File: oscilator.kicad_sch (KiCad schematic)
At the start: 5 parts, among them Y1 8Mhz

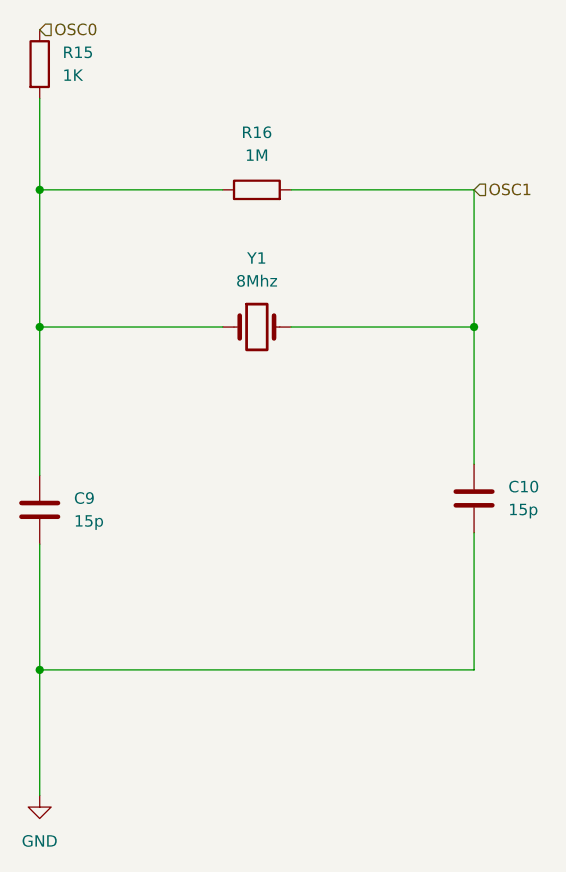
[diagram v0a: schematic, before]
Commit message: Fix KiCad 10 footprint library: register kiC library, fix schematic references
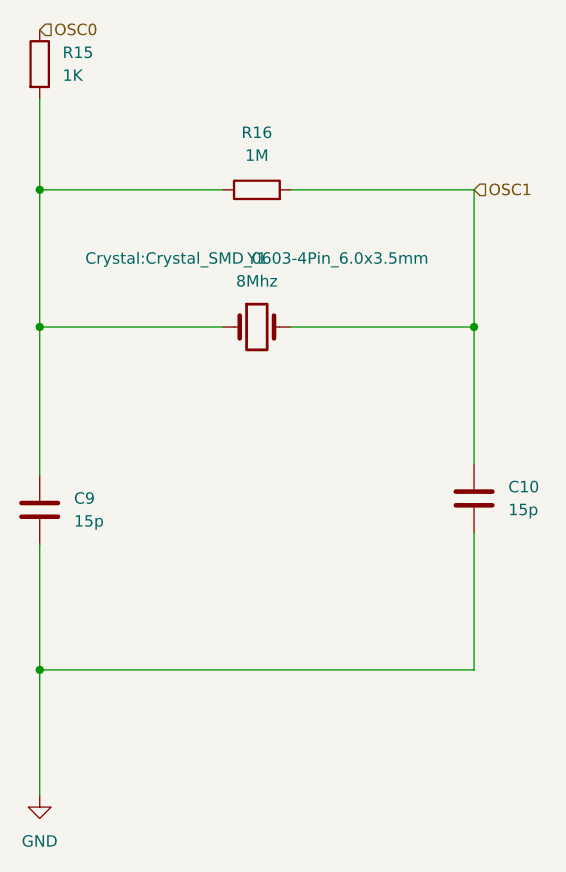
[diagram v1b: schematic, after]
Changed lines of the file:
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@@
 		(dnp no)
 		(fields_autoplaced yes)
+		(property "Footprint" "Crystal:Crystal_SMD_0603-4Pin_6.0x3.5mm"
+			(at 151.13 80.01 0)
+			(show_name no)
+			(do_not_autoplace no)
+			(effects
+				(font
+					(size 1.27 1.27)
+				)
+			)
+		)
 		(property "Reference" "Y1"
 			(at 151.13 80.01 0)

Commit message: Fix Y1/J17 footprints, update PCB and schematics
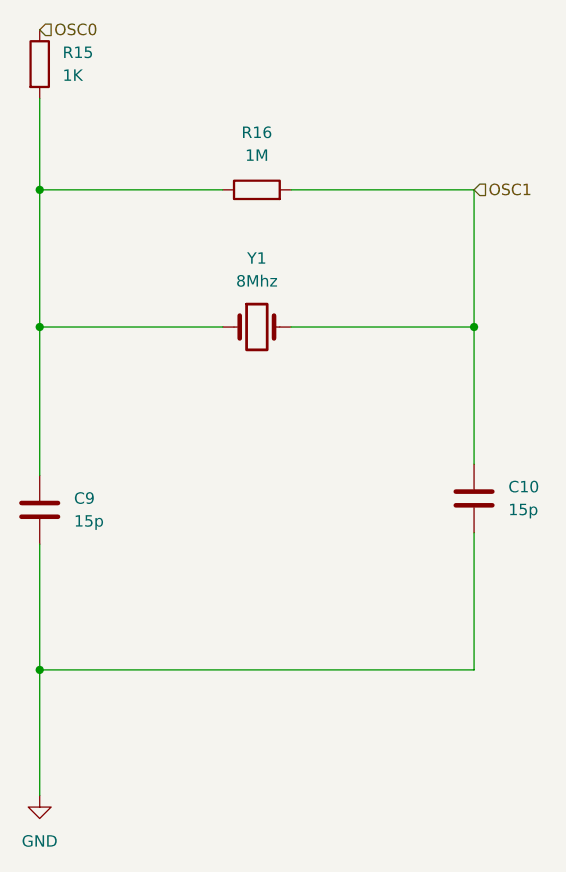
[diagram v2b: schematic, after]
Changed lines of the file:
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@@
 		(dnp no)
 		(fields_autoplaced yes)
-		(property "Footprint" "Crystal:Crystal_SMD_0603-4Pin_6.0x3.5mm"
-			(at 151.13 80.01 0)
-			(show_name no)
-			(do_not_autoplace no)
-			(effects
-				(font
-					(size 1.27 1.27)
-				)
-			)
-		)
 		(property "Reference" "Y1"
 			(at 151.13 80.01 0)
